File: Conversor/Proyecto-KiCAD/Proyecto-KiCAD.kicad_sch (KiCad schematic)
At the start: 51 parts, among them Q1 IRFP150, Q2 IRFP150, Q3 IRFP150, Q4 IRFP150, U1 UCC21540, U2 UCC21540

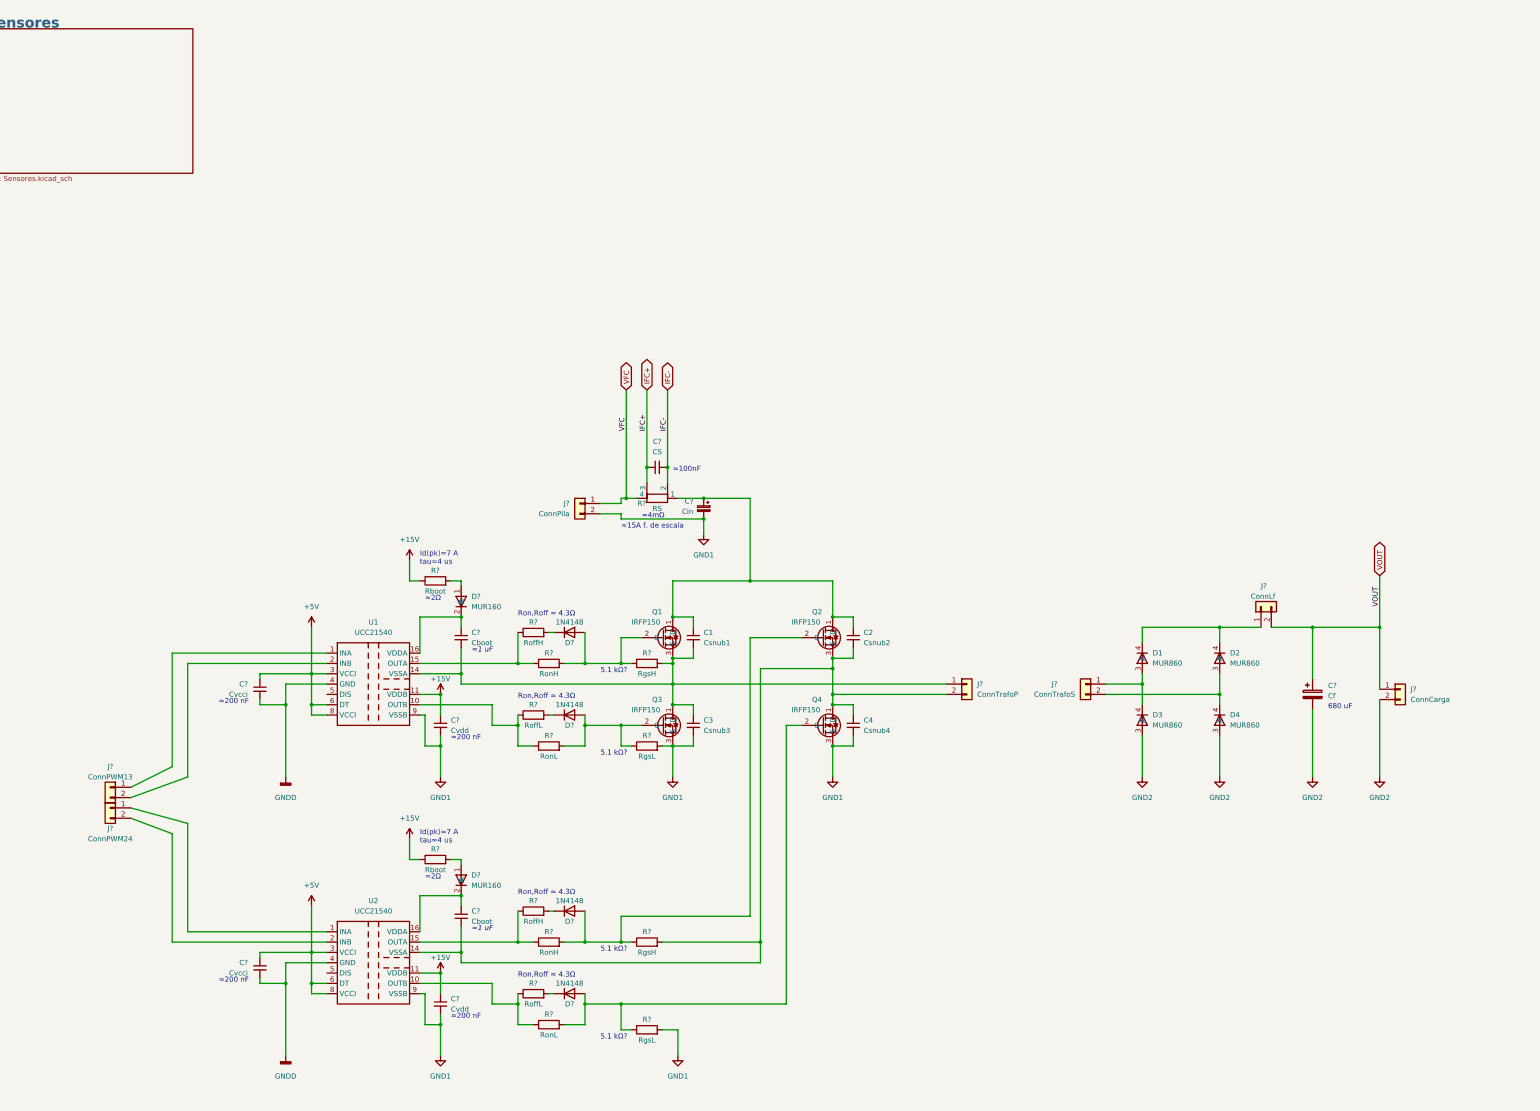
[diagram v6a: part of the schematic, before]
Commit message: Seguir con el esquematico de los sensores
- Terminadas las conexiones del LM5056A para Iin/Vin/Vout
- Para el sensor de efecto hall ACS709, falta el acondicionamiento:
  - La tension de salida para 0A (Quiescent output voltage) es Vcc/2=2.5V.
  - Para X20BB, 4.5A (Imax+10%) se traducen a 252mV y 344 valores del ADC
    (osea de 2.5V a 2.752V).
  - Para X6BB, 4.5A se traducen a 474mV y 647 valores del ADC.
    (osea de 2.5V a 2.974V)
  - Preguntar si conviene restarle 2.5V y luego amplificar la señal a los
    3V del ADC para aumentar la resolucion, o quedarse con los 250/500 mV.
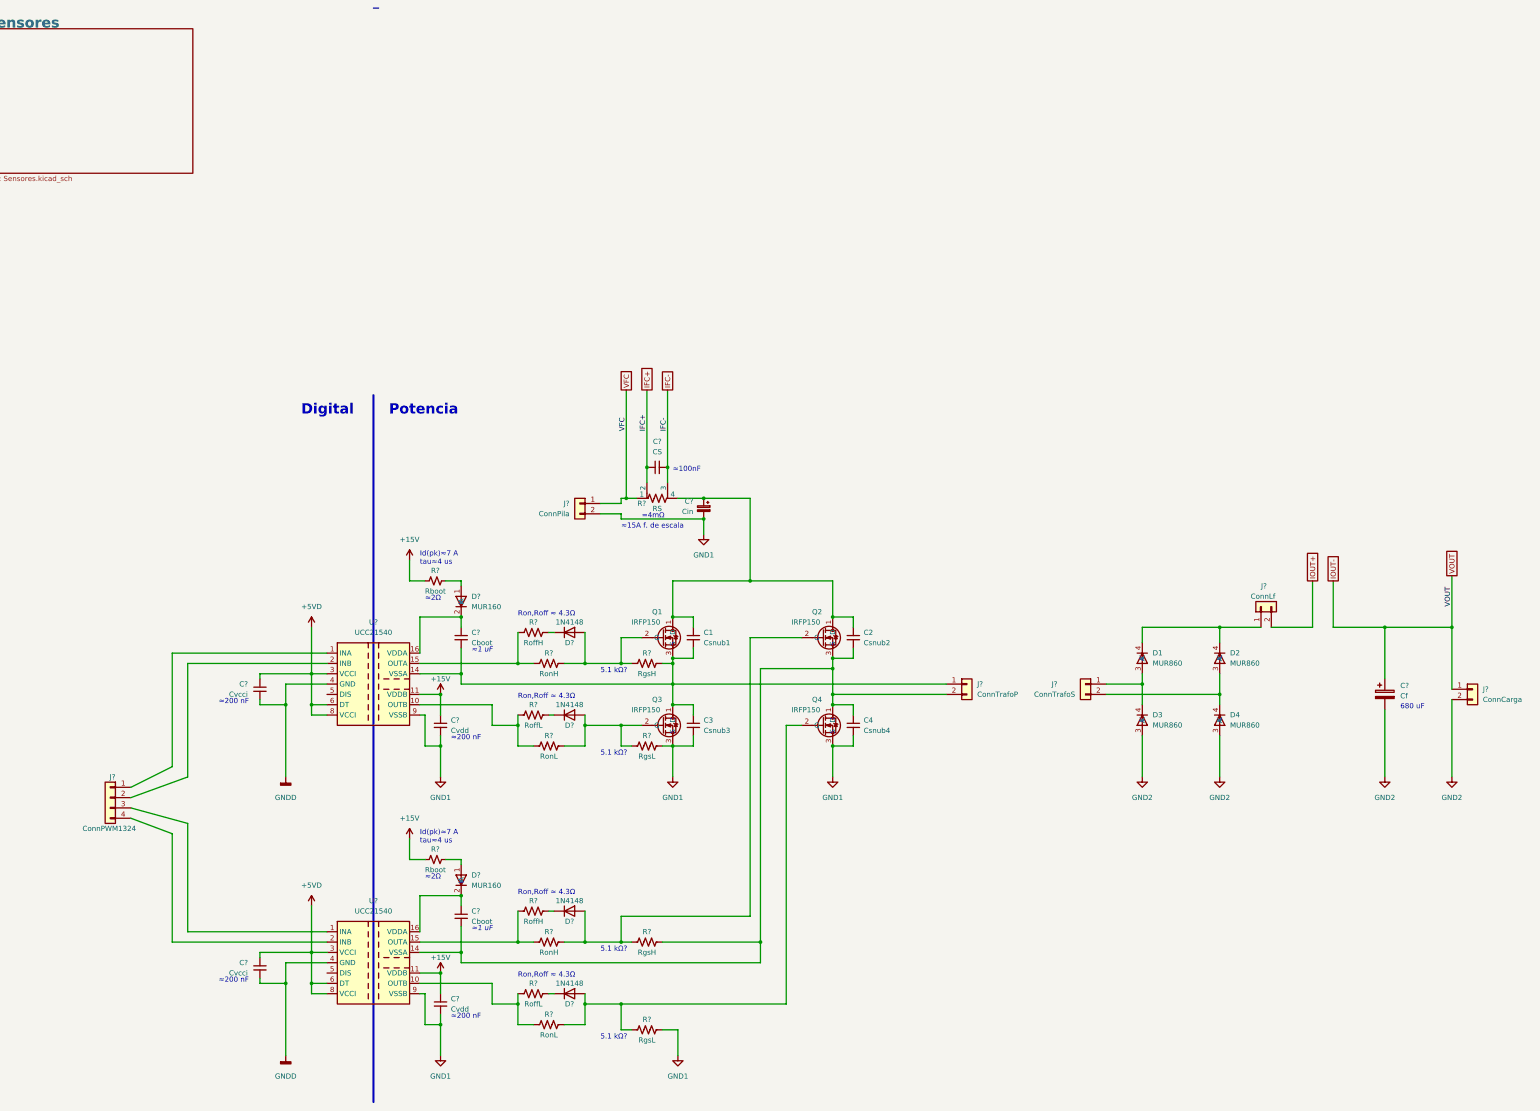
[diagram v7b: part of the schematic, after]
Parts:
- removed J?: ConnPWM24, symbol Connector_Generic:Conn_01x02
- removed J?: ConnPWM13, symbol Connector_Generic:Conn_01x02
- removed R? (x2): RonL, symbol Device:R
- removed R? (x2): Rboot, symbol Device:R
- removed R? (x2): RoffH, symbol Device:R
- removed R? (x2): RonH, symbol Device:R
- removed R?: RS, symbol Device:R_Shunt
- removed R? (x2): RgsL, symbol Device:R
- removed R? (x2): RgsH, symbol Device:R
- removed R? (x2): RoffL, symbol Device:R
- removed U1, U2: UCC21540, Package_SO:SOIC-16W_7.5x10.3mm_P1.27mm, symbol Componentes proyecto:UCC21540
- added J?: ConnPWM1324, symbol Connector_Generic:Conn_01x04
- added R? (x2): RgsL, symbol Device:R_US
- added R? (x2): RoffL, symbol Device:R_US
- added R? (x2): RonH, symbol Device:R_US
- added R? (x2): RoffH, symbol Device:R_US
- added R? (x2): Rboot, symbol Device:R_Small_US
- added R?: RS, symbol Device:R_Shunt_US
- added R? (x2): RgsH, symbol Device:R_US
- added R? (x2): RonL, symbol Device:R_US
- added U? (x2): UCC21540, symbol Componentes proyecto:UCC21540
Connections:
- net +15V: now also R?.1, R?.1, U?.11 (VDDB), U?.11 (VDDB)
- net GND1: now also R?.2, R?.2, U?.9 (VSSB), U?.9 (VSSB)
- net GNDD: now also U?.4 (GND), U?.4 (GND)
- net IFC+: now also R?.2
- net IFC-: now also R?.3
- net VFC: now also R?.1
- net at D?.1 (A): now also R?.2 (x2)
- net at C?.1, D?.2 (K): now also U?.16 (VDDA) (x2)
- net at C2.2, C4.1, C?.2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: now also R?.2, U?.14 (VSSA)
- net at D?.1 (K): now also R?.2 (x4)
- net at D?.2 (A), Q1.2 (G): now also R?.1, R?.2
- net at D?.2 (A), Q4.2 (G): now also R?.1, R?.2
- net at D?.2 (A), Q3.2 (G): now also R?.1, R?.2
- net at C1.1, C2.1, C?.1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: now also R?.4
- net at C1.2, C3.1, C?.2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: now also R?.2, U?.14 (VSSA)
- net at D?.2 (A), Q2.2 (G): now also R?.1, R?.2
- net +5V renamed +5VD
- net +5VD: now also U?.3 (VCCI), U?.3 (VCCI), U?.6 (DT), U?.6 (DT), U?.8 (VCCI), U?.8 (VCCI)
- net VOUT renamed IOUT-
- net IOUT-: no longer J?.2 (Pin_2)
- new net: R?.1, R?.1, U?.10 (OUTB) (x2)
- new net: R?.1, R?.1, U?.15 (OUTA) (x2)
- new net: J?.3 (Pin_3), U?.1 (INA)
- new net: J?.4 (Pin_4), U?.2 (INB)
- new net: J?.1 (Pin_1), U?.1 (INA)
- new net: J?.2 (Pin_2), U?.2 (INB)
- new net IOUT+: J?.2 (Pin_2)
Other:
- note added: "Digital"
- note added: "Potencia"
- moved on the sheet: C?, J?

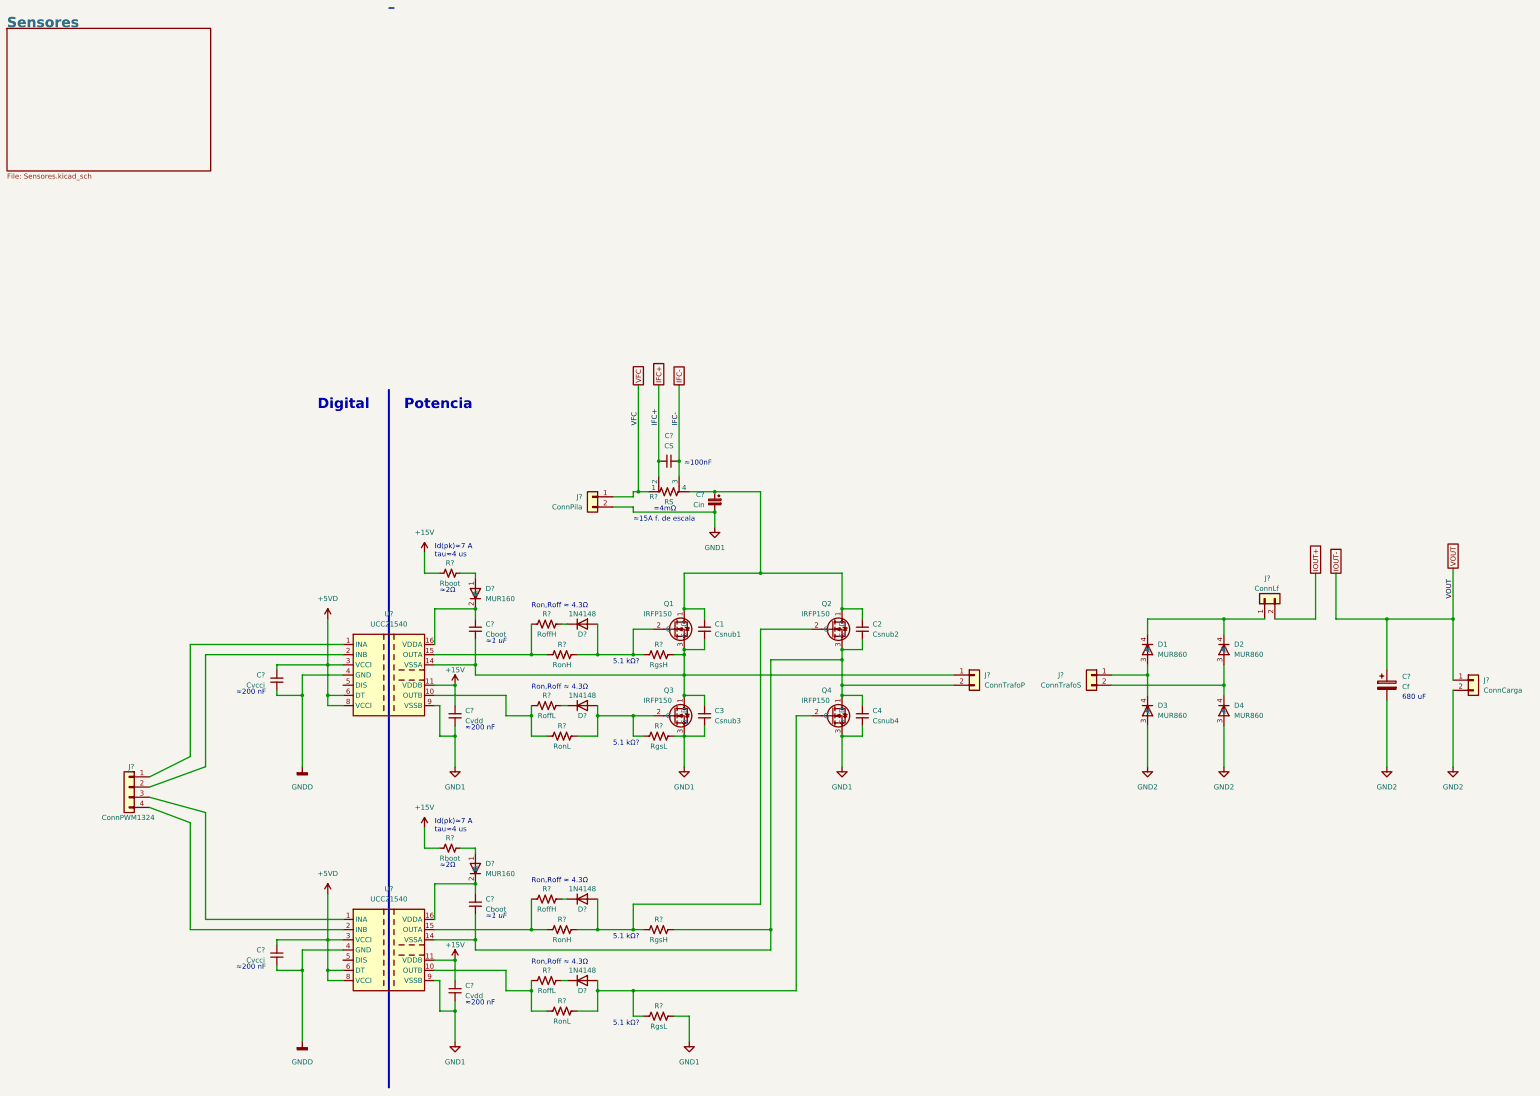
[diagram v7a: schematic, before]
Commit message: Casi terminada la parte de sensores (faltan valores)
- Faltan valores del circuito de acondicionamiento del ACS709 (difference amp.).
- Ver si se usa el mismo TLC2272 que en el diseño de referencia (agregada su datasheet).
- Agregada la bibliografia usada para entender el circuito de acondicionamiento.
- Agregadas las footprints de los integrados.
- Creada la sheet para las fuentes de alimentación.
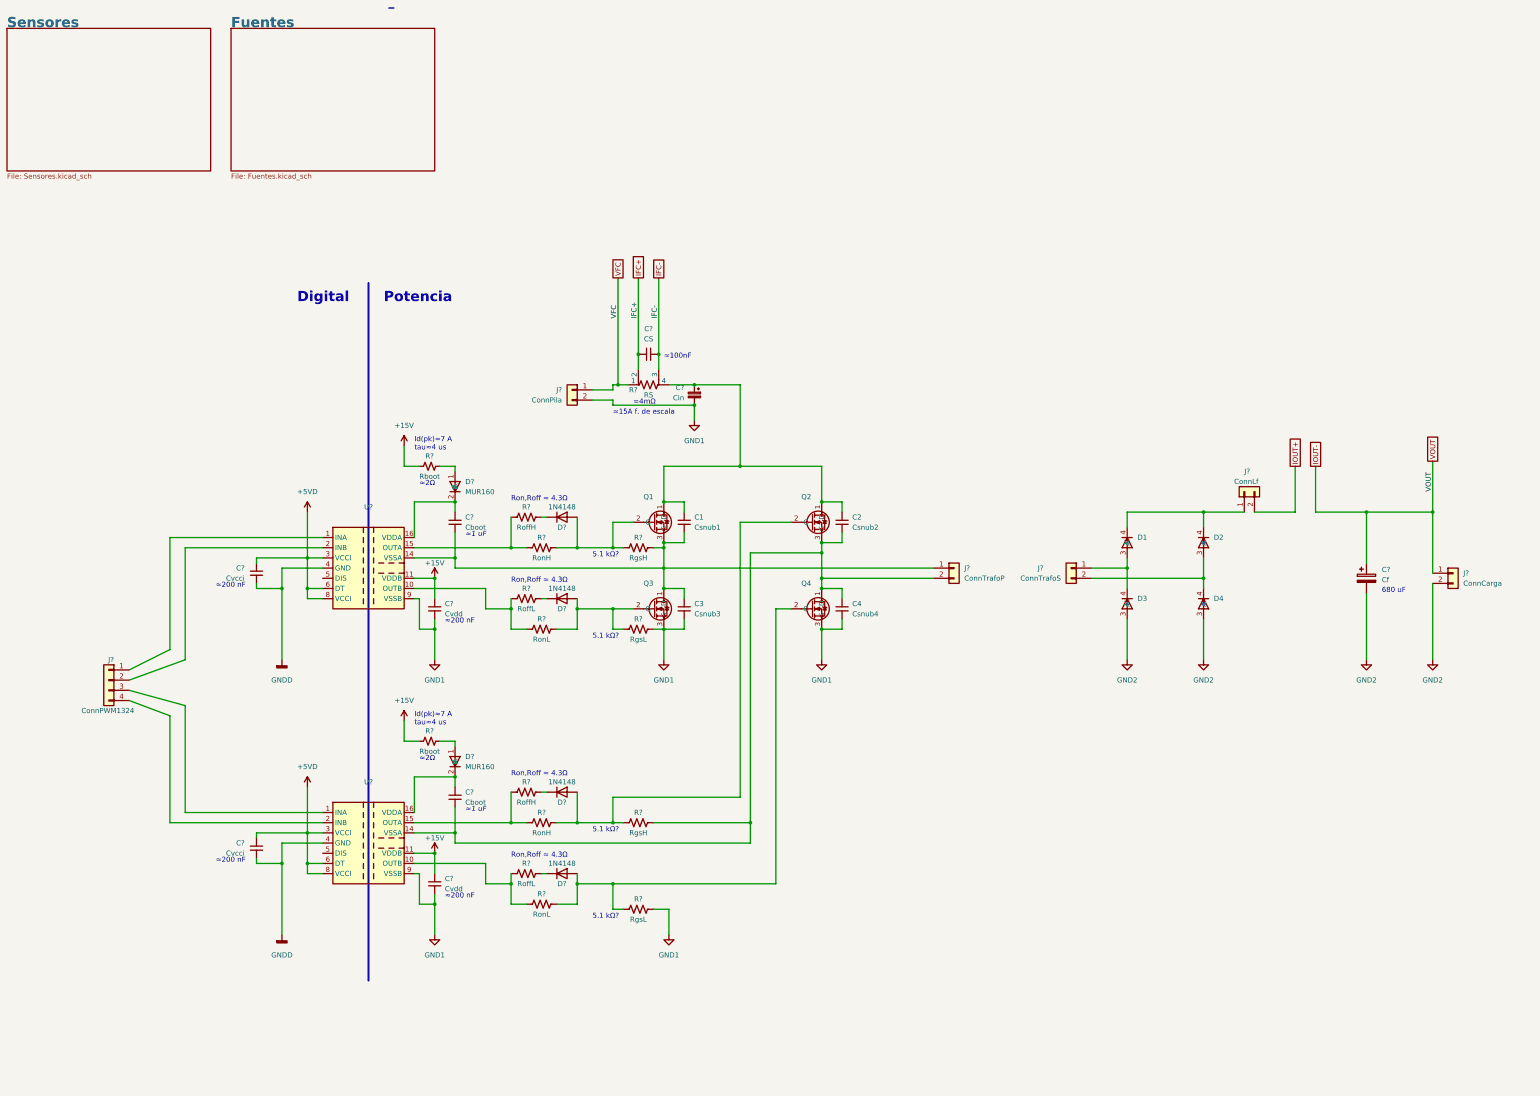
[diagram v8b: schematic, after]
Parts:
- D1, D2, D3, D4: value MUR860 -> (none)
- Q1, Q2, Q3, Q4: value IRFP150 -> (none)
- U? (x2): value UCC21540 -> (none)
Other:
- added sheet Fuentes (Fuentes.kicad_sch)
- moved on the sheet: C1, C2, C3, C4, C?, D1, D2, D3, D4, D?, J?, Q1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
